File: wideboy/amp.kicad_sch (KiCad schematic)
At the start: 31 parts, among them U14 AMP-AGB

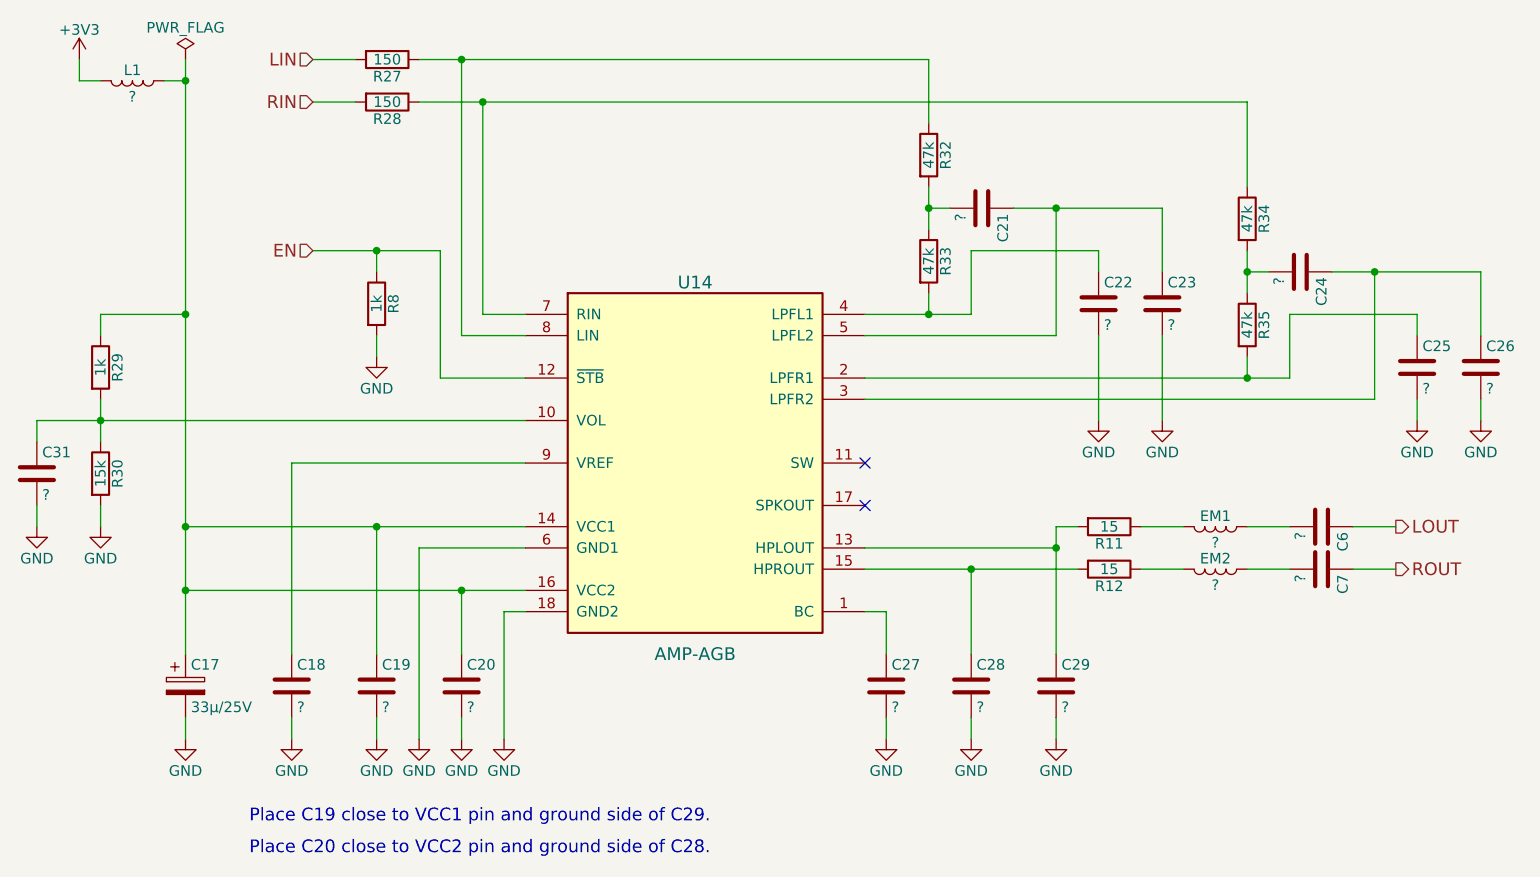
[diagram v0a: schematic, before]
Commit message: Add values for capacitors and diodes
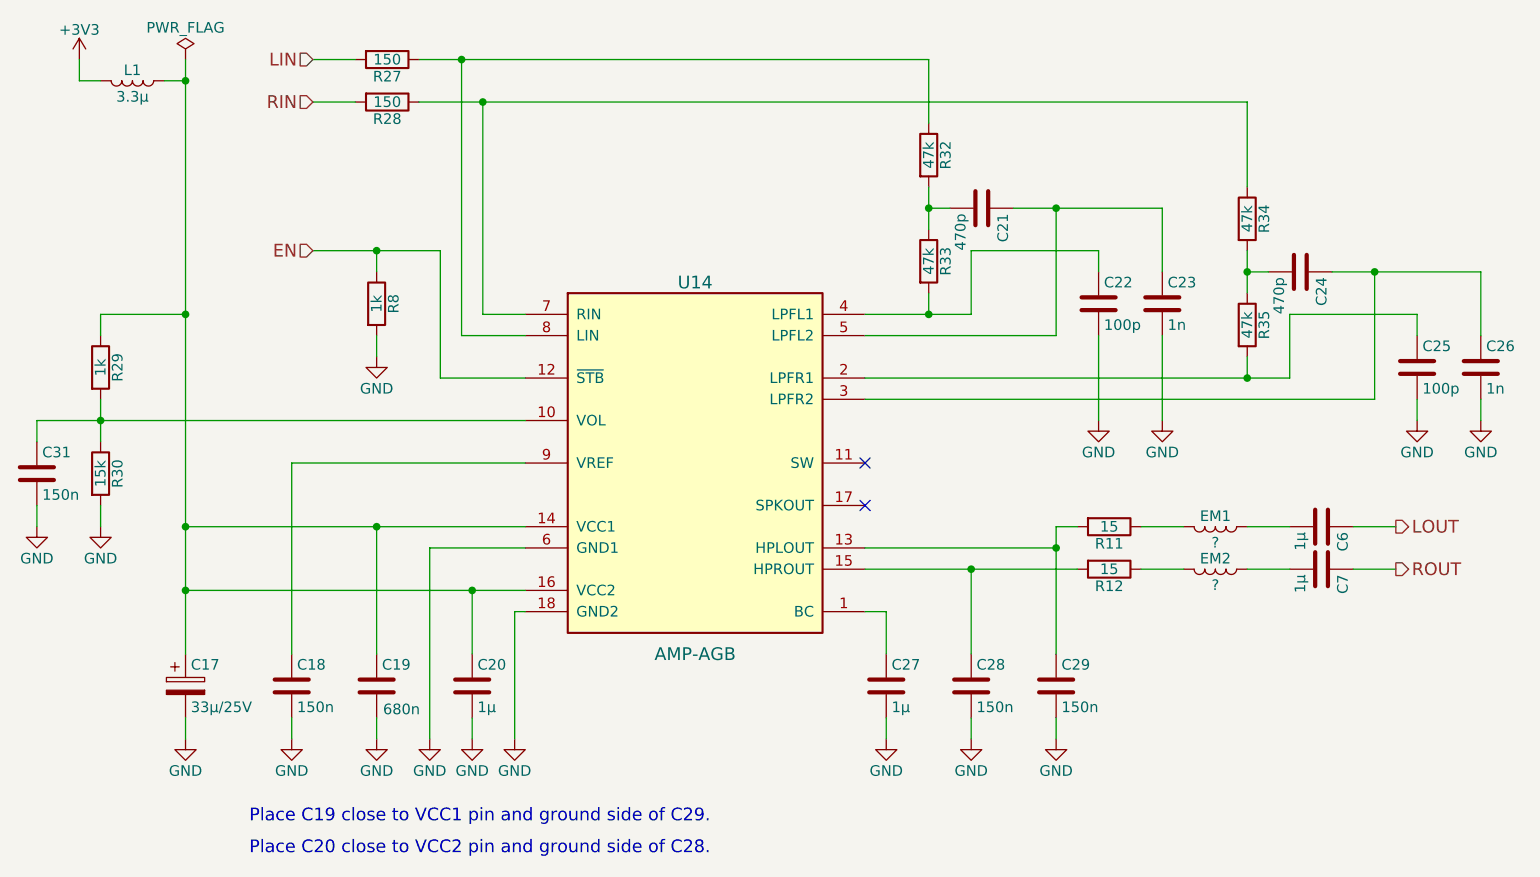
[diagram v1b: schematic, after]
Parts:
- C18, C28, C29, C31: value ? -> 150n
- C19: value ? -> 680n
- C20, C27, C6, C7: value ? -> 1µ
- C21, C24: value ? -> 470p
- C22, C25: value ? -> 100p
- C23, C26: value ? -> 1n
- L1: value ? -> 3.3µ
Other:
- moved on the sheet: C20
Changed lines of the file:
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@@
 	(title_block
 		(title "Wide-Boy64 AGB")
-		(date "2024-06-20")
-		(rev "2")
+		(date "2024-09-22")
+		(rev "3")
 		(company "CC-BY-SA-4.0 Michael Singer")
 		(comment 1 "https://github.com/msinger/wideboy/")
@@
 	)
 	(junction
-		(at 119.38 106.68)
-		(diameter 0)
-		(color 0 0 0 0)
-	)
-	(junction
 		(at 86.36 99.06)
 		(diameter 0)
@@
 		(color 0 0 0 0)
 	)
+	(junction
+		(at 120.65 106.68)
+		(diameter 0)
+		(color 0 0 0 0)
+	)
 	(no_connect
 		(at 167.64 91.44)
@@
 	(wire
 		(pts
-			(xy 127 101.6) (xy 114.3 101.6)
+			(xy 127 101.6) (xy 115.57 101.6)
 		)
 		(stroke
@@
 	(wire
 		(pts
-			(xy 124.46 109.22) (xy 124.46 124.46)
+			(xy 125.73 109.22) (xy 125.73 124.46)
 		)
 		(stroke
@@
 	(wire
 		(pts
-			(xy 114.3 101.6) (xy 114.3 124.46)
+			(xy 115.57 101.6) (xy 115.57 124.46)
 		)
 		(stroke
@@
 	(wire
 		(pts
-			(xy 119.38 106.68) (xy 127 106.68)
+			(xy 120.65 106.68) (xy 127 106.68)
 		)
 		(stroke
@@
 	(wire
 		(pts
-			(xy 86.36 106.68) (xy 119.38 106.68)
+			(xy 86.36 106.68) (xy 120.65 106.68)
 		)
 		(stroke
@@
 	(wire
 		(pts
-			(xy 127 109.22) (xy 124.46 109.22)
+			(xy 127 109.22) (xy 125.73 109.22)
 		)
 		(stroke
@@
 	(wire
 		(pts
-			(xy 119.38 106.68) (xy 119.38 114.3)
+			(xy 120.65 106.68) (xy 120.65 114.3)
 		)
 		(stroke
@@
 	(wire
 		(pts
-			(xy 119.38 121.92) (xy 119.38 124.46)
+			(xy 120.65 121.92) (xy 120.65 124.46)
 		)
 		(stroke
@@
 	(symbol
 		(lib_id "Device:C")
-		(at 119.38 118.11 0)
+		(at 120.65 118.11 0)
 		(unit 1)
 		(exclude_from_sim no)
@@
 		(dnp no)
 		(property "Reference" "C20"
-			(at 120.015 115.57 0)
+			(at 121.285 115.57 0)
 			(effects
 				(font
@@
 			)
 		)
-		(property "Value" "?"
-			(at 120.015 120.65 0)
+		(property "Value" "1µ"
+			(at 121.285 120.65 0)
 			(effects
 				(font
@@
 		)
 		(property "Footprint" ""
-			(at 120.3452 121.92 0)
+			(at 121.6152 121.92 0)
 			(effects
 				(font
@@
 		)
 		(property "Datasheet" "~"
-			(at 119.38 118.11 0)
+			(at 120.65 118.11 0)
 			(effects
 				(font
@@
 		)
 		(property "Description" "Unpolarized capacitor"
-			(at 119.38 118.11 0)
+			(at 120.65 118.11 0)
 			(effects
 				(font
@@
 			)
 		)
-		(property "Value" "?"
-			(at 109.855 120.65 0)
+		(property "Value" "680n"
+			(at 109.982 120.904 0)
 			(effects
 				(font
@@
 			)
 		)
-		(property "Value" "?"
+		(property "Value" "150n"
 			(at 99.695 120.65 0)
 			(effects
@@
 	(symbol
 		(lib_id "power:GND")
-		(at 124.46 124.46 0)
+		(at 125.73 124.46 0)
 		(unit 1)
 		(exclude_from_sim no)
@@
 		(dnp no)
 		(property "Reference" "#PWR02"
-			(at 124.46 130.81 0)
+			(at 125.73 130.81 0)
 			(effects
 				(font
@@
 		)
 		(property "Value" "GND"
-			(at 124.46 128.27 0)
+			(at 125.73 128.27 0)
 			(effects
 				(font
@@
 		)
 		(property "Footprint" ""
-			(at 124.46 124.46 0)
+			(at 125.73 124.46 0)
 			(effects
 				(font
@@
 		)
 		(property "Datasheet" ""
-			(at 124.46 124.46 0)
+			(at 125.73 124.46 0)
 			(effects
 				(font
@@
 		)
 		(property "Description" "Power symbol creates a global label with name \"GND\" , ground"
-			(at 124.46 124.46 0)
+			(at 125.73 124.46 0)
 			(effects
 				(font
@@
 	(symbol
 		(lib_id "power:GND")
-		(at 119.38 124.46 0)
+		(at 120.65 124.46 0)
 		(unit 1)
 		(exclude_from_sim no)
@@
 		(dnp no)
 		(property "Reference" "#PWR03"
-			(at 119.38 130.81 0)
+			(at 120.65 130.81 0)
 			(effects
 				(font
@@
 		)
 		(property "Value" "GND"
-			(at 119.38 128.27 0)
+			(at 120.65 128.27 0)
 			(effects
 				(font
@@
 		)
 		(property "Footprint" ""
-			(at 119.38 124.46 0)
+			(at 120.65 124.46 0)
 			(effects
 				(font
@@
 		)
 		(property "Datasheet" ""
-			(at 119.38 124.46 0)
+			(at 120.65 124.46 0)
 			(effects
 				(font
@@
 		)
 		(property "Description" "Power symbol creates a global label with name \"GND\" , ground"
-			(at 119.38 124.46 0)
+			(at 120.65 124.46 0)
 			(effects
 				(font
@@
 	(symbol
 		(lib_id "power:GND")
-		(at 114.3 124.46 0)
+		(at 115.57 124.46 0)
 		(unit 1)
 		(exclude_from_sim no)
@@
 		(dnp no)
 		(property "Reference" "#PWR04"
-			(at 114.3 130.81 0)
+			(at 115.57 130.81 0)
 			(effects
 				(font
@@
 		)
 		(property "Value" "GND"
-			(at 114.3 128.27 0)
+			(at 115.57 128.27 0)
 			(effects
 				(font
@@
 		)
 		(property "Footprint" ""
-			(at 114.3 124.46 0)
+			(at 115.57 124.46 0)
 			(effects
 				(font
@@
 		)
 		(property "Datasheet" ""
-			(at 114.3 124.46 0)
+			(at 115.57 124.46 0)
 			(effects
 				(font
@@
 		)
 		(property "Description" "Power symbol creates a global label with name \"GND\" , ground"
-			(at 114.3 124.46 0)
+			(at 115.57 124.46 0)
 			(effects
 				(font
@@
 			)
 		)
-		(property "Value" "?"
+		(property "Value" "3.3µ"
 			(at 80.01 47.625 90)
 			(effects
@@
 			)
 		)
-		(property "Value" "?"
+		(property "Value" "150n"
 			(at 69.215 95.25 0)
 			(effects
@@
 			)
 		)
-		(property "Value" "?"
+		(property "Value" "1µ"
 			(at 170.815 120.65 0)
 			(effects
@@
 			)
 		)
-		(property "Value" "?"
+		(property "Value" "150n"
 			(at 180.975 120.65 0)
 			(effects
@@
 			)
 		)
-		(property "Value" "?"
+		(property "Value" "150n"
 			(at 191.135 120.65 0)
 			(effects
@@
 			)
 		)
-		(property "Value" "?"
+		(property "Value" "1µ"
 			(at 219.71 99.695 0)
 			(effects
@@
 			)
 		)
-		(property "Value" "?"
+		(property "Value" "1µ"
 			(at 219.71 104.775 0)
 			(effects
@@
 			)
 		)
-		(property "Value" "?"
+		(property "Value" "470p"
 			(at 217.17 69.215 0)
 			(effects
@@
 			)
 		)
-		(property "Value" "?"
+		(property "Value" "1n"
 			(at 241.935 82.55 0)
 			(effects
@@
 			)
 		)
-		(property "Value" "?"
+		(property "Value" "100p"
 			(at 234.315 82.55 0)
 			(effects
@@
 			)
 		)
-		(property "Value" "?"
+		(property "Value" "470p"
 			(at 179.07 61.595 0)
 			(effects
@@
 			)
 		)
-		(property "Value" "?"
+		(property "Value" "1n"
 			(at 203.835 74.93 0)
 			(effects
@@
 			)
 		)
-		(property "Value" "?"
+		(property "Value" "100p"
 			(at 196.215 74.93 0)
 			(effects
